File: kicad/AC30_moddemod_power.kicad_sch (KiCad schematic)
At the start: 19 parts

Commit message: Wire mod/demod and external power supply; retry routing until DRC-clean
- Transcribe docs/ac30_mod_demod.pdf onto sheet 2: modulator (IC5A/B,
  IC2A, IC4A filter) and demodulator (IC4B comparator, IC3C/D edge pulses,
  carrier detect, missing-pulse detector, R16 timer, IC1A data out, 16X
  clock out). The mod/demod interface solder pads are removed.
- Transcribe docs/ac30_PS.pdf onto new sheet 3 as an external unit (no
  footprints): line cord, S6, F1, T1, bridge D14-D17, +/-13 V, +/-7.5 V
  zener rails, 7805. IC16 GND taken as GND (drawing ties it to -13 V).
- Board gets through-hole power input pads TP1-TP6 (+5V, GND, +13V, -13V,
  +7.5V, -7.5V) with rail names on the silkscreen, plus C23-C25 +5 V
  bypass. IC4 on +/-7.5 V, IC15 on +/-13 V. J2 18 VAC pins now unused.
- Corner mounting holes H1-H4, 6.35 mm in from each edge (artwork).
- Placement weighs all nets except +5V/GND; build.sh routes the placed
  board afresh up to 4 times and keeps the first DRC-clean result.
- Board 173.0 x 121.5 mm, fully routed; ERC, DRC (all severities) and
  schematic parity clean. AC30-settings.md updated.

Co-Authored-By: Claude Opus 5.5 <noreply@anthropic.com>
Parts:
- removed TP10: 18 VAC A (from J2 / T1), Connector_Wire:SolderWire-0.5sqmm_1x01_D0.9mm_OD2.1mm, symbol Connector:TestPoint
- removed TP11: 18 VAC B (from J2 / T1), Connector_Wire:SolderWire-0.5sqmm_1x01_D0.9mm_OD2.1mm, symbol Connector:TestPoint
- removed TP12: +5V (regulated), Connector_Wire:SolderWire-0.5sqmm_1x01_D0.9mm_OD2.1mm, symbol Connector:TestPoint
- removed TP13: GND (power), Connector_Wire:SolderWire-0.5sqmm_1x01_D0.9mm_OD2.1mm, symbol Connector:TestPoint
- removed TP14: RS-232 V+ (IC15 pin 14), Connector_Wire:SolderWire-0.5sqmm_1x01_D0.9mm_OD2.1mm, symbol Connector:TestPoint
- removed TP15: RS-232 V- (IC15 pin 1), Connector_Wire:SolderWire-0.5sqmm_1x01_D0.9mm_OD2.1mm, symbol Connector:TestPoint
- removed TP7: 16X CLOCK OUT (from demodulator), Connector_Wire:SolderWire-0.5sqmm_1x01_D0.9mm_OD2.1mm, symbol Connector:TestPoint
- removed TP8: CARRIER DETECT (from demodulator), Connector_Wire:SolderWire-0.5sqmm_1x01_D0.9mm_OD2.1mm, symbol Connector:TestPoint
- removed TP9: GND (mod/demod), Connector_Wire:SolderWire-0.5sqmm_1x01_D0.9mm_OD2.1mm, symbol Connector:TestPoint
- added C1, C6: 1000pF, Capacitor_THT:C_Disc_D5.0mm_W2.5mm_P5.00mm, symbol Device:C
- added C10: 2700pF, Capacitor_THT:C_Disc_D5.0mm_W2.5mm_P5.00mm, symbol Device:C
- added C11: 470pF, Capacitor_THT:C_Disc_D5.0mm_W2.5mm_P5.00mm, symbol Device:C
- added C2: 2000pF, Capacitor_THT:C_Disc_D5.0mm_W2.5mm_P5.00mm, symbol Device:C
- added C23, C24, C25: 0.1uF, Capacitor_THT:C_Disc_D5.0mm_W2.5mm_P5.00mm, symbol Device:C
- added C3, C8: 0.022uF, Capacitor_THT:C_Disc_D5.0mm_W2.5mm_P5.00mm, symbol Device:C
- added C4: 1uF 15V, Capacitor_THT:CP_Radial_D6.3mm_P2.50mm, symbol Device:C_Polarized
- added C5: 0.01uF, Capacitor_THT:C_Disc_D5.0mm_W2.5mm_P5.00mm, symbol Device:C
- added C7, C9: 0.047uF, Capacitor_THT:C_Disc_D5.0mm_W2.5mm_P5.00mm, symbol Device:C
- added D1, D2, D4: 1N4148, Diode_THT:D_DO-35_SOD27_P7.62mm_Horizontal, symbol Diode:1N4148
- added D3: 1N4732 4.7V, Diode_THT:D_DO-35_SOD27_P7.62mm_Horizontal, symbol Device:D_Zener
- added IC1, IC5: 4013, Package_DIP:DIP-14_W7.62mm, symbol 4xxx:4013
- added IC2: 4001, Package_DIP:DIP-14_W7.62mm, symbol 4xxx:4001
- added IC3: 4070, Package_DIP:DIP-14_W7.62mm, symbol 4xxx:4070
- added IC4: 4558, Package_DIP:DIP-8_W7.62mm, symbol Amplifier_Operational:RC4558
- added Q1, Q2, Q4: 2N5210, Package_TO_SOT_THT:TO-92_Inline, symbol Transistor_BJT:Q_NPN_EBC
- added Q3: 2N5087, Package_TO_SOT_THT:TO-92_Inline, symbol Transistor_BJT:Q_PNP_EBC
- added R1: 33K, Resistor_THT:R_Axial_DIN0207_L6.3mm_D2.5mm_P10.16mm_Horizontal, symbol Device:R
- added R10: 330K, Resistor_THT:R_Axial_DIN0207_L6.3mm_D2.5mm_P10.16mm_Horizontal, symbol Device:R
- added R11, R12, R15, R19, R2, R20, R21, R22, R3, R9: 10K, Resistor_THT:R_Axial_DIN0207_L6.3mm_D2.5mm_P10.16mm_Horizontal, symbol Device:R
- added R13, R14: 22K, Resistor_THT:R_Axial_DIN0207_L6.3mm_D2.5mm_P10.16mm_Horizontal, symbol Device:R
- added R16: 20K trim, Potentiometer_THT:Potentiometer_Bourns_3386P_Vertical, symbol Device:R_Potentiometer_Trim
- added R17, R18, R8: 100K, Resistor_THT:R_Axial_DIN0207_L6.3mm_D2.5mm_P10.16mm_Horizontal, symbol Device:R
- added R4: 330, Resistor_THT:R_Axial_DIN0207_L6.3mm_D2.5mm_P10.16mm_Horizontal, symbol Device:R
- added R5: 2.2K, Resistor_THT:R_Axial_DIN0207_L6.3mm_D2.5mm_P10.16mm_Horizontal, symbol Device:R
- added R6: 4.7K, Resistor_THT:R_Axial_DIN0207_L6.3mm_D2.5mm_P10.16mm_Horizontal, symbol Device:R
- added R7: 470, Resistor_THT:R_Axial_DIN0207_L6.3mm_D2.5mm_P10.16mm_Horizontal, symbol Device:R
- TP1: value DATA IN (to modulator) -> +5V
- TP2: value 16X CLOCK IN (to modulator) -> GND
- TP3: value ~{CARRIER ENABLE} (to modulator) -> +13V
- TP4: value AUDIO OUT (from modulator) -> -13V
- TP5: value AUDIO IN (to demodulator) -> +7.5V
- TP6: value DATA OUT (from demodulator) -> -7.5V
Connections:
- net +5V: now also TP1.1, C23.1, C24.1, C25.1, C7.1, IC1.14 (VDD), IC2.14 (VDD), IC3.14 (VDD), IC3.8, IC5.14 (VDD), Q3.1 (E), R1.2, R16.2, R16.3, R18.1, R22.1
- net AUDIO_IN: now also C5.1, R8.1; no longer TP5.1
- net AUDIO_OUT: now also C4.2; no longer TP4.1
- net CARRIER_DETECT: now also IC3.3
- net CARRIER_EN_N: now also IC5.10 (R); no longer TP3.1
- net CLOCK_IN: now also IC5.11 (C); no longer TP2.1
- net CLOCK_OUT: now also Q4.3 (C), R22.2
- net DATA_IN: now also IC2.1; no longer TP1.1
- net DATA_OUT: now also IC1.1 (Q); no longer TP6.1
- net GND: now also TP2.1, C2.2, C23.2, C24.2, C25.2, C6.2, C8.2, C9.2, D1.2 (A), D2.1 (K), D3.2 (A), IC1.10 (R), IC1.11 (C), IC1.4 (R), IC1.6 (S), IC1.7 (VSS), IC1.8 (S), IC1.9 (D), IC2.7 (VSS), IC3.6, IC3.7 (VSS), IC4.6 (-), IC5.6 (S), IC5.7 (VSS), IC5.8 (S), Q1.1 (E), Q2.1 (E), Q4.1 (E), R20.2, R5.2, R7.2, R8.2
- new net +13V: TP3.1
- new net +7.5V: IC4.8 (V+), TP5.1
- new net -13V: TP4.1
- new net -7.5V: IC4.4 (V-), TP6.1
- new net DEM_BIT: C10.1, IC1.5 (D), IC3.4
- new net DEM_BIT_EDGE: C10.2, IC2.13, R20.1
- new net DEM_CD: C7.2, D4.2 (A), IC3.1, IC3.2, Q3.3 (C)
- new net DEM_CLK_N: C11.1, IC2.11, R21.1
- new net DEM_CMP: IC4.7, R10.2, R11.1
- new net DEM_D4: D4.1 (K), R17.2
- new net DEM_DLY: C6.1, IC3.13, R12.2
- new net DEM_EDGE: IC2.8, IC2.9, IC3.11, R17.1
- new net DEM_HP: C5.2, R9.1
- new net DEM_IN: D1.1 (K), D2.2 (A), IC4.5 (+), R10.1, R9.2
- new net DEM_INV: IC3.10, R12.1
- new net DEM_LIM: D3.1 (K), IC3.12, IC3.9, R11.2
- new net DEM_PULSE: IC1.3 (C), IC2.10, IC2.12, R13.1, R14.1
- new net DEM_Q1B: Q1.2 (B), R13.2
- new net DEM_Q2B: Q2.2 (B), R14.2
- new net DEM_Q2C: C9.1, IC2.5, IC2.6, Q2.3 (C), R18.2
- new net DEM_Q3B: IC2.4, R19.1
- new net DEM_Q3B_R: Q3.2 (B), R19.2
- new net DEM_Q4B: C11.2, Q4.2 (B), R21.2
- new net DEM_R16: R15.2, R16.1
- new net DEM_TIMER: C8.1, IC3.5, Q1.3 (C), R15.1
- new net MOD_ATTEN: C4.1, R6.2, R7.1
- new net MOD_CLK2: C1.1, IC5.13 (Q), IC5.3 (C)
- new net MOD_DIV2_N: IC5.12 (~{Q}), IC5.9 (D)
- new net MOD_DIV4_N: IC5.2 (~{Q}), IC5.5 (D)
- new net MOD_EDGE: C1.2, IC2.2, R1.1
- new net MOD_F1: C3.1, R2.2, R3.1
- new net MOD_F2: C2.1, IC4.3 (+), R3.2
- new net MOD_FB: C3.2, R4.2, R5.1
- new net MOD_FILT: IC4.1, IC4.2 (-), R4.1, R6.1
- new net MOD_RST: IC2.3, IC5.4 (R)
- new net MOD_SQ: IC5.1 (Q), R2.1
- no-connect marks 0 -> 3
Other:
- note added: "Demodulator: comparator IC4B, edge pulses IC3C/D, carrier detect, data and 16X clock out"
- note added: "Generated from docs/ac30_mod_demod.pdf (SWTPC AC-30 Cassette Tape Modulator/Demodulator Schematic). Connectivity is by net label: identical labels are connected. Transcription notes / assumptions: - IC4 (4558) supply pins are not drawn. The assembly manual says IC4 runs from the +/-7.5 V zener rails (D12/D13 on the power supply sheet). - R16's far end has a terminal dot with no label; taken as +5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"
- note added: "Modulator: CLOCK IN /2 (IC5B), /1 or /2 by DATA IN (IC5A), 2-pole filter IC4A"
- note added: "Power input pads (from the external supply) and +5 V bypass"
- note removed: "Mod/demod interface pads"
- note removed: "Power supply pads"
- note removed: "The modulator/demodulator and power supply schematics are NOT in docs/ - only the switching schematic is. Until they are, the board brings every signal and supply that crosses into those circuits out to a labelled solder pad (TP1-TP15), so the switching section can be built and tested with an external mod/demod and supply. The mod/demod and power BOM parts are listed (not placed) in tools/netlist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"
- title: SWTPC AC-30 - Mod/Demod & Power interface pads -> SWTPC AC-30 - Modulator/Demodulator & power input
- moved on the sheet: H1, H2, H3, H4, TP1, TP2, TP3, TP4, TP5, TP6

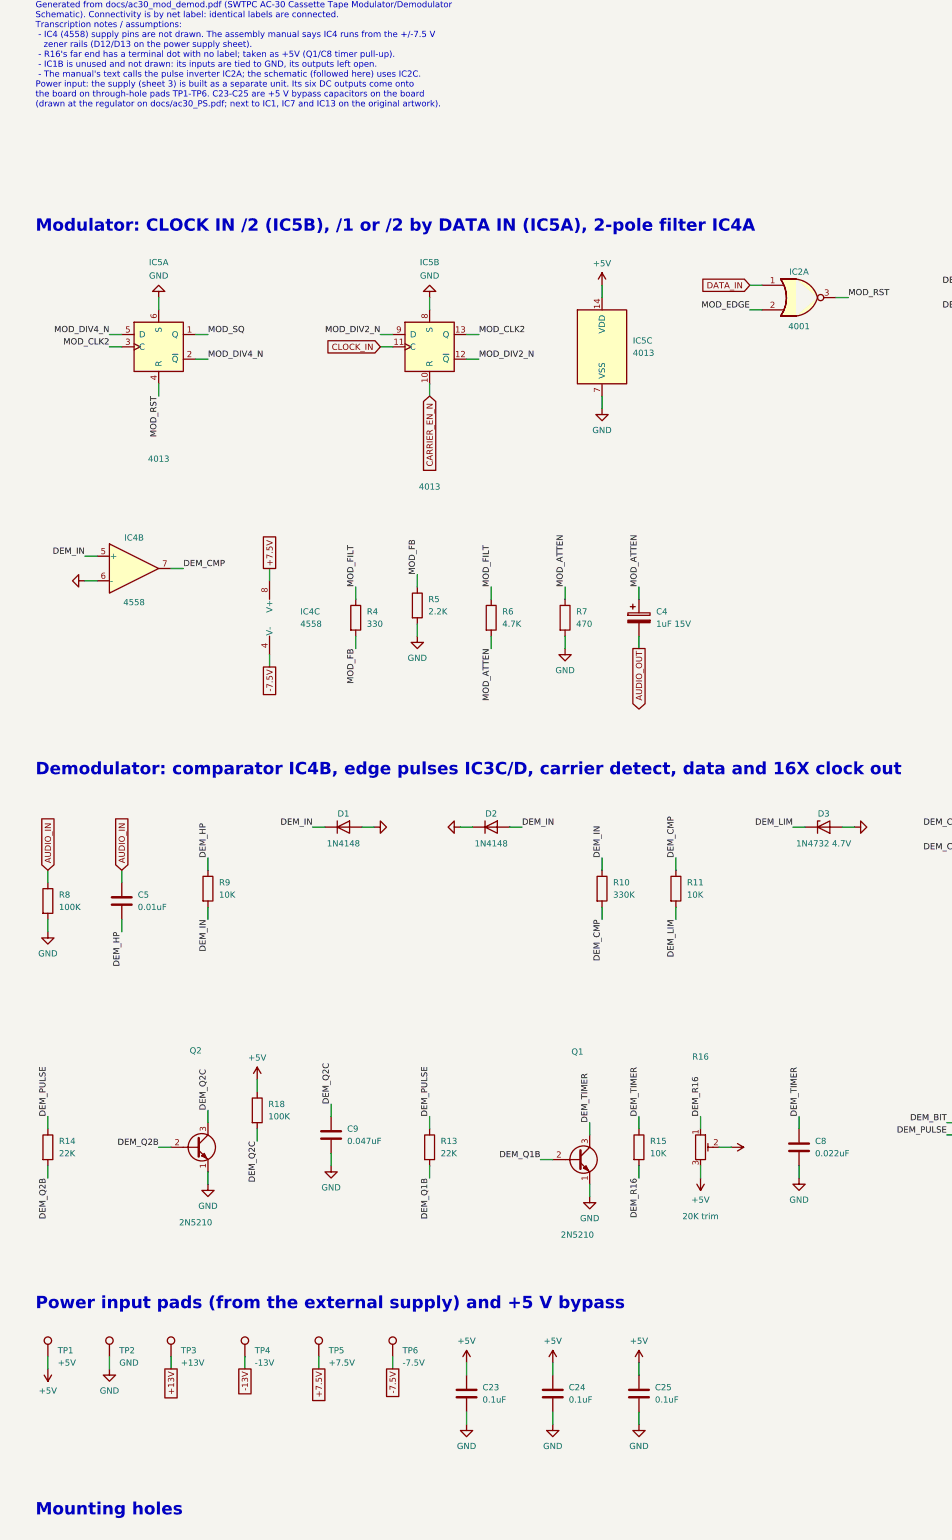
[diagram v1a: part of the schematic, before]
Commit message: Replace power input pads with J12, a 6-pin KK-396 header on the bottom edge
- J12 (Molex KK-396 A-41791-0006) replaces solder pads TP1-TP6 for the
  external supply: 1 GND, 2 +5V, 3 +13V, 4 -13V, 5 +7.5V, 6 -7.5V.
  Placed in the bottom connector row next to J2, clear of the corner hole.
- build.sh: if no routing attempt is DRC-clean, up to 3 finishing passes
  route only what is left on the best result, each checked by DRC.
- Board 173.5 x 122.0 mm, fully routed; ERC, DRC (all severities) and
  schematic parity clean. AC30-settings.md updated (power input, drill
  table, routing, positions).

Co-Authored-By: Claude Opus 5.5 <noreply@anthropic.com>
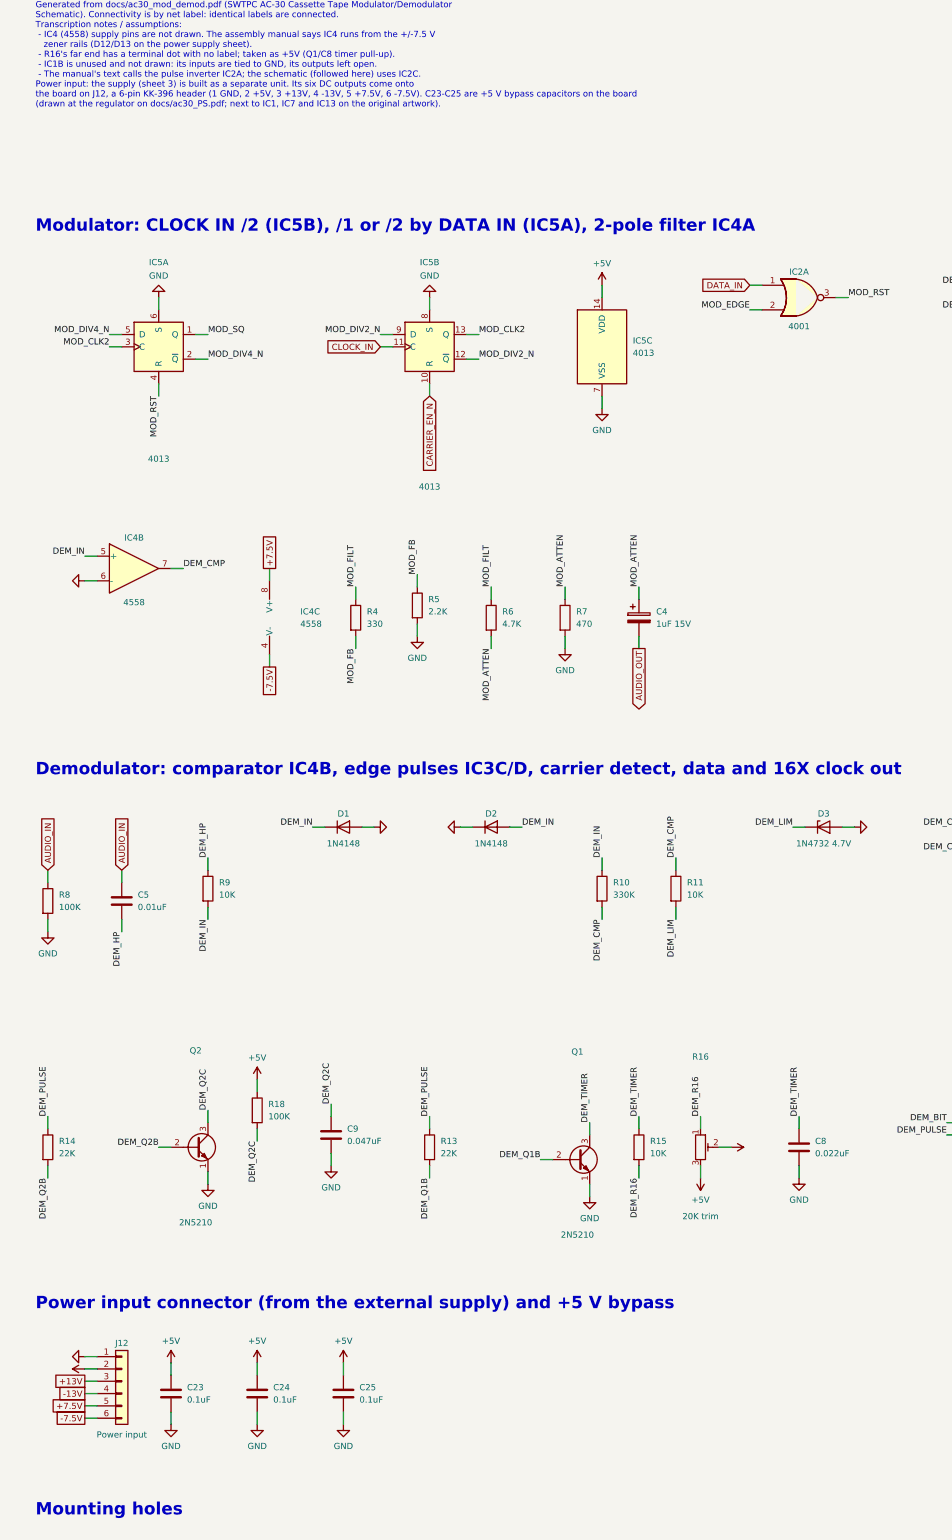
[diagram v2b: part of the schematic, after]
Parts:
- removed TP1: +5V, Connector_Wire:SolderWire-0.5sqmm_1x01_D0.9mm_OD2.1mm, symbol Connector:TestPoint
- removed TP2: GND, Connector_Wire:SolderWire-0.5sqmm_1x01_D0.9mm_OD2.1mm, symbol Connector:TestPoint
- removed TP3: +13V, Connector_Wire:SolderWire-0.5sqmm_1x01_D0.9mm_OD2.1mm, symbol Connector:TestPoint
- removed TP4: -13V, Connector_Wire:SolderWire-0.5sqmm_1x01_D0.9mm_OD2.1mm, symbol Connector:TestPoint
- removed TP5: +7.5V, Connector_Wire:SolderWire-0.5sqmm_1x01_D0.9mm_OD2.1mm, symbol Connector:TestPoint
- removed TP6: -7.5V, Connector_Wire:SolderWire-0.5sqmm_1x01_D0.9mm_OD2.1mm, symbol Connector:TestPoint
- added J12: Power input, Connector_Molex:Molex_KK-396_A-41791-0006_1x06_P3.96mm_Vertical, symbol Connector_Generic:Conn_01x06
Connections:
- net +13V: now also J12.3 (Pin_3)
- net +5V: now also J12.2 (Pin_2)
- net +7.5V: now also J12.5 (Pin_5)
- net -13V: now also J12.4 (Pin_4)
- net -7.5V: now also J12.6 (Pin_6)
- net GND: now also J12.1 (Pin_1)
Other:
- note added: "Power input connector (from the external supply) and +5 V bypass"
- note removed: "Power input pads (from the external supply) and +5 V bypass"
- moved on the sheet: C23, C24, C25

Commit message: Wired, human-readable schematics with PDF and PNG images
gen.py now lays out each functional group on its own and draws its nets
as real wires (new tools/schroute.py: orthogonal grid router that never
ends, bends or overlaps on another net's wire); every routed net keeps
one label with its name, labels join nets between blocks and sheets, and
unroutable connections fall back to label pairs (17). The front-panel
jumper pads share the front-panel block. Custom 1488/1489 output pins
moved onto the 2.54 mm grid.

build.sh exports schematic/<project>.pdf and, via tools/schimg.py, PNGs
of every sheet and functional block for both boards.

Connectivity unchanged (pin-to-net maps identical for both variants);
ERC 0; both PCBs DRC/parity clean and unchanged. Docs updated.

Co-Authored-By: Claude Opus 5.5 <noreply@anthropic.com>
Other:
- note added: "Generated from docs/ac30_mod_demod.pdf (SWTPC AC-30 Cassette Tape Modulator/Demodulator Schematic). Each block is wired; net labels join the blocks and sheets (identical labels are connected). Transcription notes / assumptions: - IC4 (4558) supply pins are not drawn. The assembly manual says IC4 runs from the +/-7.5 V zener rails (D12/D13 on the power supply sheet). - R16's far end has a terminal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"
- note removed: "Generated from docs/ac30_mod_demod.pdf (SWTPC AC-30 Cassette Tape Modulator/Demodulator Schematic). Connectivity is by net label: identical labels are connected. Transcription notes / assumptions: - IC4 (4558) supply pins are not drawn. The assembly manual says IC4 runs from the +/-7.5 V zener rails (D12/D13 on the power supply sheet). - R16's far end has a terminal dot with no label; taken as +5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"
- moved on the sheet: C1, C10, C11, C2, C23, C24, C25, C3, C4, C5, C6, C7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
